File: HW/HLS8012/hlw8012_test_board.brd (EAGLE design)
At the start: 29.5 x 72.4 mm, 36 parts, among them T2 2N3904, T3 2N3904, T4 2N3904

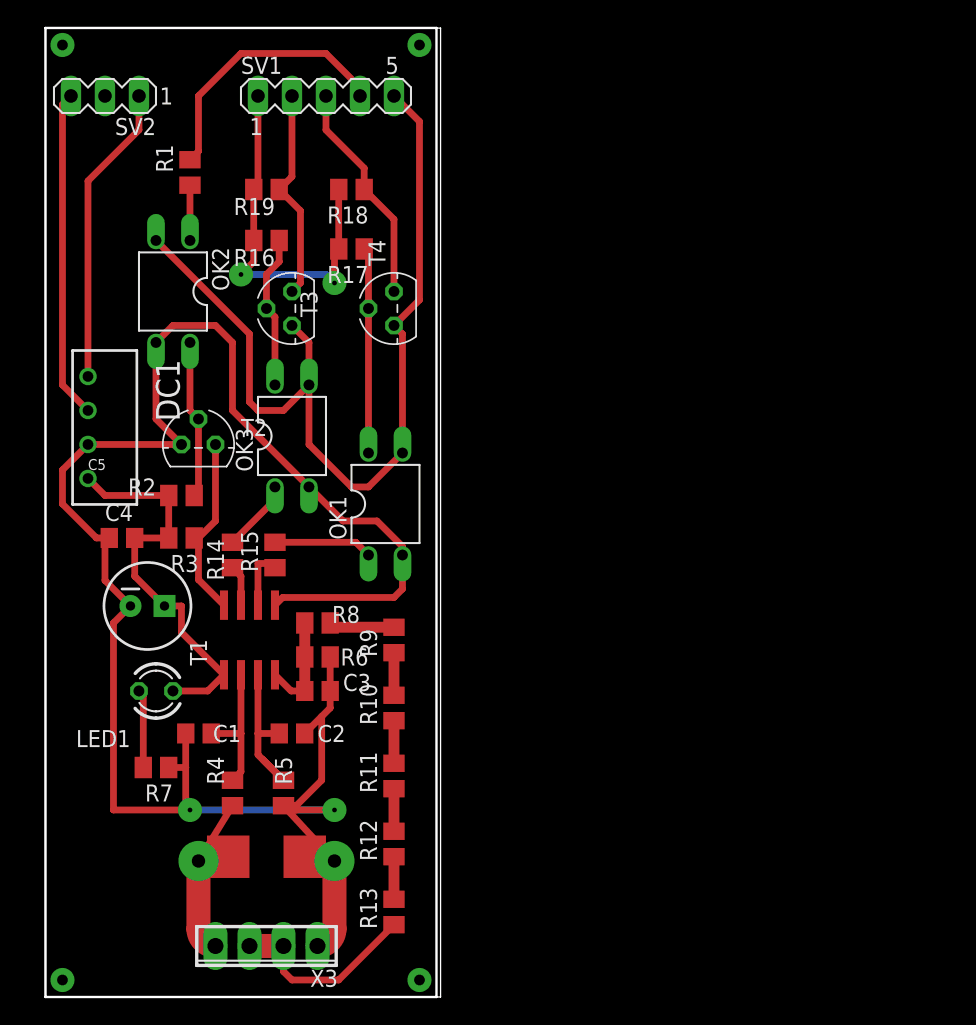
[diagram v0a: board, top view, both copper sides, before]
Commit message: Refactored hlw board
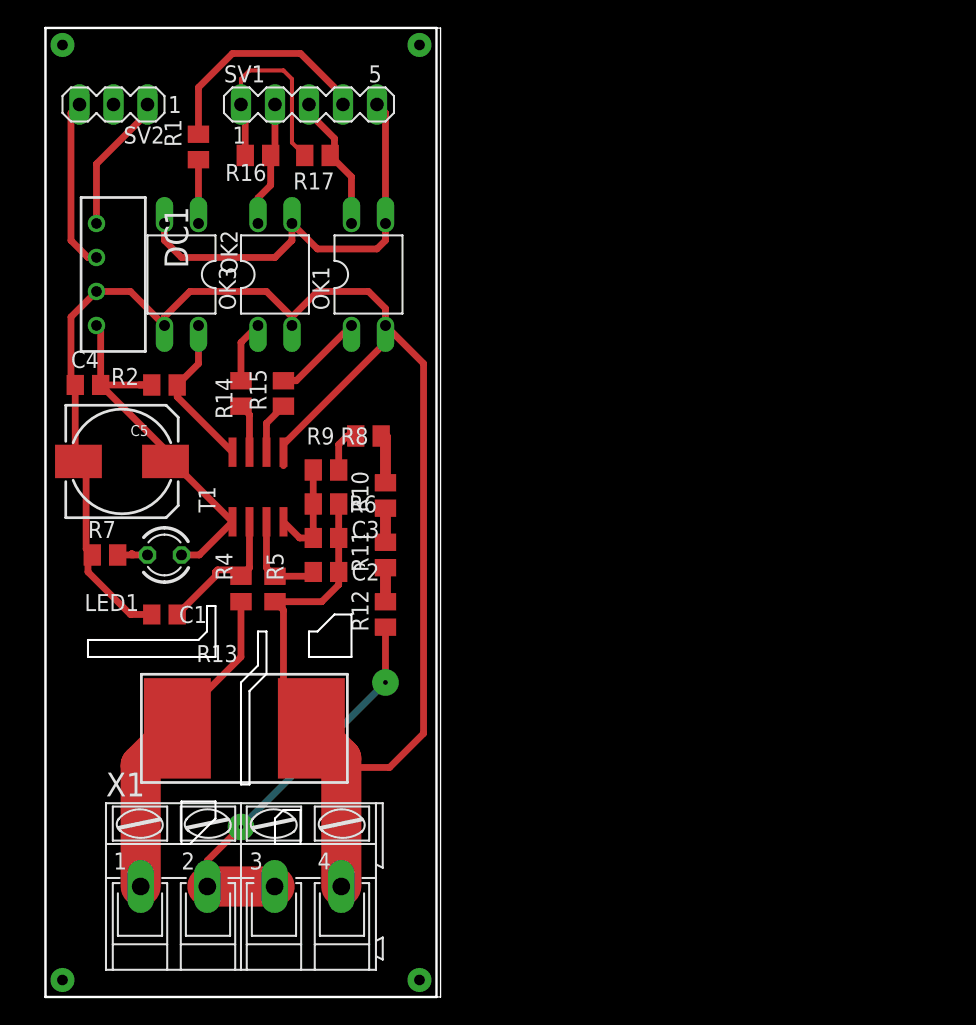
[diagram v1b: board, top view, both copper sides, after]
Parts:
- removed R18, R19, R3: 20K, rcl:M0805
- removed T2, T3, T4: 2N3904, transistor:TO92
- removed X3: (no value), con-phoenix-254:4POL254
- added X1: (no value), con-ptr500:AK300/4
- C5: value (none) -> 100nF; device antduino:SPARKFUN_CPOL-RADIAL-100UF-25V -> rcl:153CLV-0810
- R13: value 470 -> (none); device rcl:M0805 -> resistor-shunt:PMD
- moved R13 18.1 mm to (16.5, 21.0), turned to 0 degrees
- moved OK1 17.2 mm to (26.0, 54.6)
- moved R12 17.2 mm to (27.3, 29.2)
- moved R11 16.5 mm to (27.3, 33.7)
- moved R7 16.3 mm to (6.35, 33.7), turned to 0 degrees
- moved R10 15.9 mm to (27.3, 38.1)
- moved R9 15.4 mm to (26.0, 42.5), turned to 180 degrees
- moved R4 15.3 mm to (16.5, 31.1)
- moved R5 15.3 mm to (19.1, 31.1)
- moved C2 12.3 mm to (22.9, 32.4)
- moved OK3 12.1 mm to (19.1, 54.6)
- moved R14 12.1 mm to (16.5, 45.7)
- moved R15 12.1 mm to (19.7, 45.7)
- moved C4 11.7 mm to (5.08, 46.4)
- moved R6 11.4 mm to (22.9, 37.5)
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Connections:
- removed net N$11: OK1.4, R17.1, T4.2
- removed net N$13: R19.1, SV1.2, T3.1
- removed net N$29: R12.1, R13.2
- removed net N$5: R3.1, T1.8, T2.1
- net GND: now also C5.-, R13.1, X1.4; no longer C5.2, T2.3, X3.1
- net N$1: no longer R18.2, R19.2
- net N$12: now also OK1.4, R17.1; no longer R18.1, T4.1
- net N$16: no longer T3.3, T4.3
- net N$17: now also R13.2, X1.1; no longer X3.4
- net N$30: now also R12.1, X1.2, X1.3; no longer R13.1, X3.2, X3.3
- net N$4: now also T1.8; no longer T2.2
- net N$6: now also SV1.2; no longer T3.2
- net VDD: now also C5.+; no longer C5.1, R3.2
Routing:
- net N$16: track 67.7 -> 31.6 mm
- net N$13: track 15.9 -> 0.00 mm
- net N$11: track 15.4 -> 0.00 mm
- net N$30: track 14.7 -> 29.9 mm, vias 0 -> 2
- net N$5: track 13.8 -> 0.00 mm
- net N$14: track 22.5 -> 10.5 mm
- net N$15: track 24.5 -> 12.9 mm
- net N$1: track 28.2 -> 17.2 mm, vias 2 -> 0
- net N$17: track 11.7 -> 22.5 mm
- net N$12: track 16.7 -> 11.1 mm
- net N$20: track 12.5 -> 7.33 mm
- net N$18: track 5.85 -> 2.34 mm
- net N$29: track 3.18 -> 0.00 mm
- net N$2: track 20.1 -> 17.3 mm
- net N$6: track 11.5 -> 9.42 mm
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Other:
- outline, holes or cut-outs redrawn

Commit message: Updated hlw board. Added libs
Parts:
- removed OK1: PC817, optocoupler:DIL04
- removed R15: 0.5K, rcl:M0805
- removed R17: 10K, rcl:M0805
- C5: value 100nF -> 10uF; device rcl:153CLV-0810 -> rcl:153CLV-0405
- DC1: value VA-1205S -> VA-0505S1
- R16: value 10K -> 2K
- R2: value 10K -> 5K
- moved SV2 58.4 mm to (8.38, 8.89), turned to 270 degrees
- moved SV1 48.2 mm to (8.26, 21.0), turned to 90 degrees
- moved DC1 47.4 mm to (17.7, 8.76), flipped to the bottom, turned to 180 degrees
- moved R1 45.1 mm to (12.6, 19.1), turned to 180 degrees
- moved C4 43.2 mm to (25.9, 8.51), turned to 90 degrees
- moved X1 42.0 mm to (58.0, 14.9), turned to 90 degrees
- moved R16 40.2 mm to (11.6, 23.7), turned to 270 degrees
- moved OK2 39.7 mm to (19.1, 15.5), flipped to the bottom, turned to 90 degrees
- moved C5 38.6 mm to (29.7, 9.02), turned to 90 degrees
- moved R2 36.4 mm to (26.7, 13.6), turned to 270 degrees
- moved R7 36.4 mm to (33.8, 9.78), turned to 90 degrees
- moved R12 31.2 mm to (58.4, 27.4), turned to 180 degrees
- moved C1 31.0 mm to (37.2, 13.0), turned to 90 degrees
- moved R4 30.4 mm to (38.2, 9.91), turned to 180 degrees
- moved R13 29.9 mm to (45.7, 14.6), turned to 90 degrees
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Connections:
- removed net N$10: R15.1, T1.6
- removed net N$12: OK1.4, R17.1, SV1.3
- removed net N$8: OK3.1, R14.2
- net GND: no longer OK1.2, OK3.2
- net N$1: now also OK2.1; no longer R17.2
- net N$16: no longer OK1.3, OK2.2
- net N$2: now also OK2.2, R1.1; no longer R1.2, SV1.4
- net N$3: now also R1.2, SV1.2; no longer OK2.1, R1.1
- net N$6: now also SV1.4; no longer SV1.2
- net N$7: now also OK3.2, R14.2; no longer OK1.1, R15.2
- net VDD: now also OK3.1
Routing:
- net GND: track 141.6 -> 88.8 mm, vias 0 -> 2
- net N$16: track 31.6 -> 14.4 mm
- net N$2: track 17.3 -> 3.00 mm
- net N$12: track 11.1 -> 0.00 mm
- net VDD: track 29.0 -> 37.9 mm, vias 0 -> 2
- net N$30: track 29.9 -> 22.5 mm, vias 2 -> 0
- net N$21: track 7.81 -> 13.8 mm
- net N$4: track 12.3 -> 6.53 mm
- net N$5: track 3.70 -> 8.50 mm
- net N$8: track 4.66 -> 0.00 mm
- net N$10: track 3.96 -> 0.00 mm
- net N$14: track 10.5 -> 6.57 mm
- net N$15: track 12.9 -> 9.00 mm
- net N$1: track 17.2 -> 21.0 mm
- net N$17: track 22.5 -> 19.9 mm
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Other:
- board size 29.5 x 72.4 mm -> 68.9 x 30.6 mm
